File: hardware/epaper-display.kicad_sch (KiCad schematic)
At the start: 51 parts, among them J1 AES200200A00 FPC, J2 USB-C, J3 LiPo JST-PH, J4 I2C temp (optional), J5 UART, J6 GPIO expansion, Q1 Si1304BDL / NX3008NBK, SW1 EN/RESET, SW2 BOOT, U1 ESP32-S3-WROOM-1-N8, U2 MCP73831T-2ACI/OT, U3 MCP1825S-3302E/DB

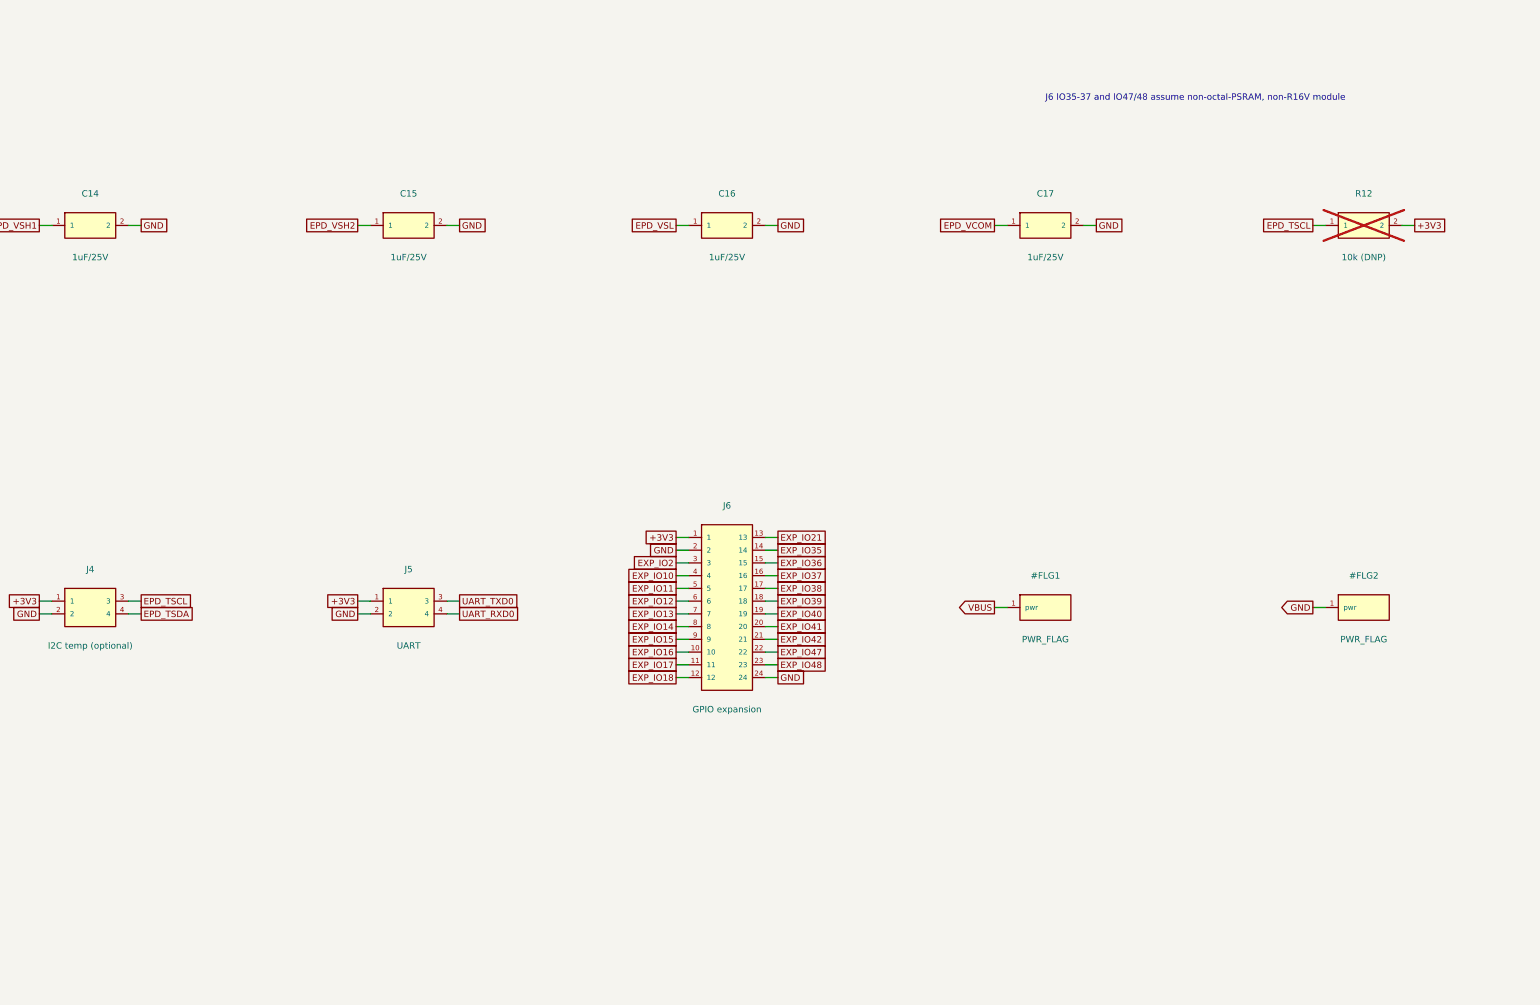
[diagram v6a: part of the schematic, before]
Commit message: hardware: stabilize schematic note generation
Co-Authored-By: Devin AI <158243242+devin-ai-integration[bot]@users.noreply.github.com>
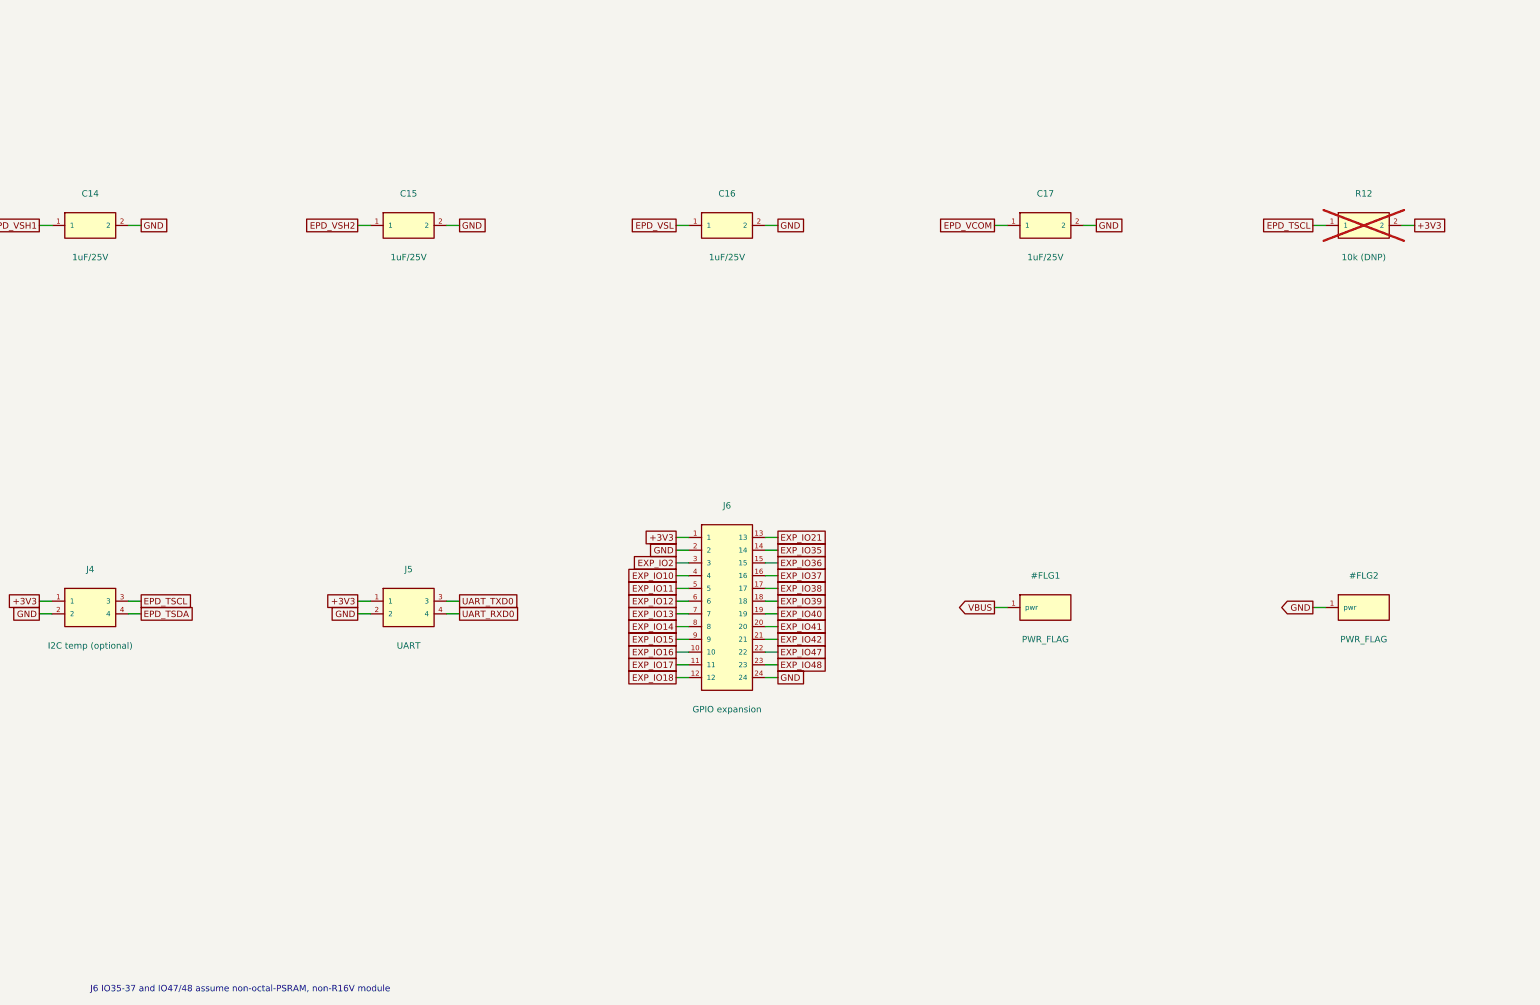
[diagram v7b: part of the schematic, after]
